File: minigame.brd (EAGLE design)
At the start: 98.7 x 80 mm, 37 parts, among them J1 AVR_SPI_PRG_6PTH, U1 MCP73831, U2 MIC5219 3.3V, Y1 8MHz

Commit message: Vista preliminar de la placa (BRD)
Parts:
- moved C6 105.0 mm to (35.6, 26.7)
- moved C7 100.4 mm to (30.5, 19.1)
- moved C8 99.8 mm to (30.5, 14.0)
- moved C9 99.8 mm to (30.5, 10.2)
- moved R11 92.6 mm to (26.7, 27.9)
- moved Y1 87.0 mm to (48.3, 33.0)
- moved U2 86.1 mm to (12.7, 29.2)
- moved R3 73.8 mm to (25.4, 58.4)
- moved R2 69.2 mm to (25.4, 62.2)
- moved C4 69.1 mm to (5.08, 30.5)
- moved C5 64.9 mm to (6.35, 16.5)
- moved R1 64.8 mm to (25.4, 66.0)
- moved U1 62.7 mm to (6.35, 24.1)
- moved J1 60.8 mm to (22.9, 72.4)
- moved R10 57.6 mm to (5.08, 8.89)
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
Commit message: ERC
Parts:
- LED1: value (none) -> RED
- OLED128X64: value (none) -> ADAFRUIT-938
- POWER: value (none) -> ON/OFF
- renumbered OLED128X64-938 to OLED128X64
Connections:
- removed net N$3: R1.1, S1.3, U$1.13
- net GND: now also BAT1.2; no longer BAT1.3
- net RST: now also R1.1, S1.3, U$1.13
- net VBAT: now also BAT1.3; no longer BAT1.2
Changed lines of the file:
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@@
 <element name="J1" library="SparkFun-Connectors" package="2X3" value="AVR_SPI_PRG_6PTH" x="22.86" y="72.39"/>
 <element name="JP1" library="SparkFun-Connectors" package="USB-MINIB-NOSTOP" value="USB-SMD-NS" x="49.53" y="5.08" rot="R90"/>
-<element name="LED1" library="SparkFun-LED" package="LED-0603" value="" x="6.35" y="60.96"/>
-<element name="OLED128X64-938" library="SparkFun-Connectors" package="1X08_LONGPADS" value="" x="38.1" y="68.58"/>
+<element name="LED1" library="SparkFun-LED" package="LED-0603" value="RED" x="6.35" y="60.96"/>
+<element name="OLED128X64" library="SparkFun-Connectors" package="1X08_LONGPADS" value="ADAFRUIT-938" x="38.1" y="68.58"/>
 <element name="R1" library="rcl" package="M0805" value="10k" x="25.4" y="66.04"/>
 <element name="R2" library="rcl" package="M0805" value="22" x="25.4" y="62.23"/>
@@
 <element name="R8" library="rcl" package="M0805" value="10k" x="20.32" y="7.62"/>
 <element name="R9" library="rcl" package="M0805" value="10k" x="20.32" y="3.81"/>
-<element name="POWER" library="SparkFun-Electromechanical" package="AYZ0202" value="" x="90.17" y="7.62">
+<element name="POWER" library="SparkFun-Electromechanical" package="AYZ0202" value="ON/OFF" x="90.17" y="7.62">
 <attribute name="PROD_ID" value="SWCH-08179" x="90.17" y="7.62" size="1.778" layer="27" display="off"/>
 </element>
@@
 <contactref element="R6" pad="1"/>
 <contactref element="R5" pad="1"/>
-<contactref element="BAT1" pad="3"/>
 <contactref element="U1" pad="2"/>
 <contactref element="R10" pad="2"/>
@@
 <contactref element="C9" pad="1"/>
 <contactref element="C8" pad="1"/>
-<wire x1="52.79" y1="49.72" x2="69.85" y2="66.04" width="0" layer="19" extent="1-1"/>
+<contactref element="BAT1" pad="2"/>
+<wire x1="52.79" y1="49.72" x2="82.55" y2="66.04" width="0" layer="19" extent="1-16"/>
 <wire x1="50.19" y1="51.52" x2="52.79" y2="49.72" width="0" layer="19" extent="1-1"/>
 <wire x1="43.79" y1="51.52" x2="50.19" y2="51.52" width="0" layer="19" extent="1-1"/>
@@
 <wire x1="45.39" y1="39.92" x2="41.19" y2="46.52" width="0" layer="19" extent="1-1"/>
 <wire x1="52.79" y1="41.72" x2="45.39" y2="39.92" width="0" layer="19" extent="1-1"/>
-<wire x1="19.37" y1="22.86" x2="45.39" y2="39.92" width="0" layer="19" extent="1-1"/>
-<wire x1="19.37" y1="19.05" x2="19.37" y2="22.86" width="0" layer="19" extent="1-1"/>
+<wire x1="33.16" y1="26.67" x2="45.39" y2="39.92" width="0" layer="19" extent="1-1"/>
+<wire x1="29.08" y1="19.05" x2="33.16" y2="26.67" width="0" layer="19" extent="1-1"/>
+<wire x1="29.08" y1="13.97" x2="29.08" y2="19.05" width="0" layer="19" extent="1-1"/>
+<wire x1="29.08" y1="10.16" x2="29.08" y2="13.97" width="0" layer="19" extent="1-1"/>
+<wire x1="19.37" y1="19.05" x2="29.08" y2="19.05" width="0" layer="19" extent="1-1"/>
+<wire x1="19.37" y1="22.86" x2="19.37" y2="19.05" width="0" layer="19" extent="1-1"/>
 <wire x1="19.37" y1="15.24" x2="19.37" y2="19.05" width="0" layer="19" extent="1-1"/>
 <wire x1="19.37" y1="11.43" x2="19.37" y2="15.24" width="0" layer="19" extent="1-1"/>
 <wire x1="19.37" y1="7.62" x2="19.37" y2="11.43" width="0" layer="19" extent="1-1"/>
 <wire x1="19.37" y1="3.81" x2="19.37" y2="7.62" width="0" layer="19" extent="1-1"/>
-<wire x1="51.13" y1="7.58" x2="19.37" y2="7.62" width="0" layer="19" extent="1-1"/>
-<wire x1="6.096" y1="76.835" x2="43.79" y2="51.52" width="0" layer="19" extent="1-1"/>
-<wire x1="15.11" y1="58.42" x2="6.096" y2="76.835" width="0" layer="19" extent="1-1"/>
-<wire x1="15.11" y1="62.23" x2="15.11" y2="58.42" width="0" layer="19" extent="1-1"/>
-<wire x1="15.11" y1="66.04" x2="15.11" y2="62.23" width="0" layer="19" extent="1-1"/>
-<wire x1="27.94" y1="74.93" x2="15.11" y2="58.42" width="0" layer="19" extent="1-1"/>
-<wire x1="6.35" y1="22.8299" x2="27.94" y2="74.93" width="0" layer="19" extent="1-1"/>
-<wire x1="6.03" y1="8.89" x2="6.35" y2="22.8299" width="0" layer="19" extent="1-1"/>
-<wire x1="3.68" y1="30.48" x2="6.03" y2="8.89" width="0" layer="19" extent="1-1"/>
-<wire x1="3.95" y1="16.51" x2="3.68" y2="30.48" width="0" layer="19" extent="1-1"/>
-<wire x1="12.7" y1="27.9099" x2="3.95" y2="16.51" width="0" layer="19" extent="1-1"/>
-<wire x1="33.16" y1="26.67" x2="12.7" y2="27.9099" width="0" layer="19" extent="1-1"/>
-<wire x1="29.08" y1="19.05" x2="33.16" y2="26.67" width="0" layer="19" extent="1-1"/>
-<wire x1="29.08" y1="13.97" x2="29.08" y2="19.05" width="0" layer="19" extent="1-1"/>
-<wire x1="29.08" y1="10.16" x2="29.08" y2="13.97" width="0" layer="19" extent="1-1"/>
+<wire x1="12.7" y1="27.9099" x2="19.37" y2="22.86" width="0" layer="19" extent="1-1"/>
+<wire x1="6.35" y1="22.8299" x2="12.7" y2="27.9099" width="0" layer="19" extent="1-1"/>
+<wire x1="3.95" y1="16.51" x2="6.35" y2="22.8299" width="0" layer="19" extent="1-1"/>
+<wire x1="6.03" y1="8.89" x2="3.95" y2="16.51" width="0" layer="19" extent="1-1"/>
+<wire x1="3.68" y1="30.48" x2="6.35" y2="22.8299" width="0" layer="19" extent="1-1"/>
+<wire x1="51.13" y1="7.58" x2="29.08" y2="10.16" width="0" layer="19" extent="1-1"/>
+<wire x1="27.94" y1="74.93" x2="43.79" y2="51.52" width="0" layer="19" extent="1-1"/>
+<wire x1="15.11" y1="66.04" x2="27.94" y2="74.93" width="0" layer="19" extent="1-1"/>
+<wire x1="15.11" y1="62.23" x2="15.11" y2="66.04" width="0" layer="19" extent="1-1"/>
+<wire x1="15.11" y1="58.42" x2="15.11" y2="62.23" width="0" layer="19" extent="1-1"/>
+<wire x1="6.096" y1="76.835" x2="15.11" y2="66.04" width="0" layer="19" extent="1-1"/>
 </signal>
 <signal name="3.3V">
@@
 <wire x1="6.48" y1="30.48" x2="7.3" y2="25.4301" width="0" layer="19" extent="1-1"/>
 </signal>
-<signal name="N$3">
-<contactref element="R1" pad="1"/>
-<contactref element="S1" pad="3"/>
-<contactref element="U$1" pad="13"/>
-<wire x1="24.45" y1="66.04" x2="6.096" y2="73.025" width="0" layer="19" extent="1-1"/>
-<wire x1="43.79" y1="39.92" x2="24.45" y2="66.04" width="0" layer="19" extent="1-1"/>
-</signal>
 <signal name="D-">
 <contactref element="R2" pad="1"/>
@@
 <signal name="RST">
 <contactref element="J1" pad="5"/>
+<contactref element="R1" pad="1"/>
+<contactref element="S1" pad="3"/>
+<contactref element="U$1" pad="13"/>
+<wire x1="24.45" y1="66.04" x2="27.94" y2="72.39" width="0" layer="19" extent="1-1"/>
+<wire x1="6.096" y1="73.025" x2="24.45" y2="66.04" width="0" layer="19" extent="1-1"/>
+<wire x1="43.79" y1="39.92" x2="24.45" y2="66.04" width="0" layer="19" extent="1-1"/>
 </signal>
 <signal name="MOSI">
@@
 </signal>
 <signal name="OLED_DATA">
-<contactref element="OLED128X64-938" pad="1"/>
+<contactref element="OLED128X64" pad="1"/>
 </signal>
 <signal name="OLED_CLK">
-<contactref element="OLED128X64-938" pad="2"/>
+<contactref element="OLED128X64" pad="2"/>
 </signal>
 <signal name="OLED_DC">
-<contactref element="OLED128X64-938" pad="3"/>
+<contactref element="OLED128X64" pad="3"/>
 </signal>
 <signal name="OLED_RST">
-<contactref element="OLED128X64-938" pad="4"/>
+<contactref element="OLED128X64" pad="4"/>
 </signal>
 <signal name="OLED_CS">
-<contactref element="OLED128X64-938" pad="5"/>
+<contactref element="OLED128X64" pad="5"/>
 </signal>
 <signal name="OLED_3V3">
-<contactref element="OLED128X64-938" pad="6"/>
+<contactref element="OLED128X64" pad="6"/>
 </signal>
 <signal name="OLED_VIN">
-<contactref element="OLED128X64-938" pad="7"/>
+<contactref element="OLED128X64" pad="7"/>
 </signal>
 <signal name="OLED_GND">
-<contactref element="OLED128X64-938" pad="8"/>
+<contactref element="OLED128X64" pad="8"/>
 </signal>
 <signal name="UP">
@@
 <wire x1="5.4" y1="25.4301" x2="4.13" y2="8.89" width="0" layer="19" extent="1-1"/>
 </signal>
-<signal name="VBAT">
-<contactref element="U1" pad="3"/>
-<contactref element="BAT1" pad="2"/>
-<contactref element="C5" pad="+"/>
-<contactref element="POWER" pad="2"/>
-<wire x1="90.17" y1="10.445" x2="82.55" y2="66.04" width="0" layer="19" extent="1-16"/>
-<wire x1="8.75" y1="16.51" x2="90.17" y2="10.445" width="0" layer="19" extent="1-1"/>
-<wire x1="7.3" y1="22.8299" x2="8.75" y2="16.51" width="0" layer="19" extent="1-1"/>
-</signal>
 <signal name="CHARGE">
 <contactref element="U$1" pad="32"/>
@@
 <wire x1="13.65" y1="30.5101" x2="31.88" y2="19.05" width="0" layer="19" extent="1-1"/>
 </signal>
+<signal name="VBAT">
+<contactref element="U1" pad="3"/>
+<contactref element="C5" pad="+"/>
+<contactref element="POWER" pad="2"/>
+<contactref element="BAT1" pad="3"/>
+<wire x1="90.17" y1="10.445" x2="69.85" y2="66.04" width="0" layer="19" extent="1-1"/>
+<wire x1="7.3" y1="22.8299" x2="69.85" y2="66.04" width="0" layer="19" extent="1-1"/>
+<wire x1="8.75" y1="16.51" x2="7.3" y2="22.8299" width="0" layer="19" extent="1-1"/>
+</signal>
 </signals>

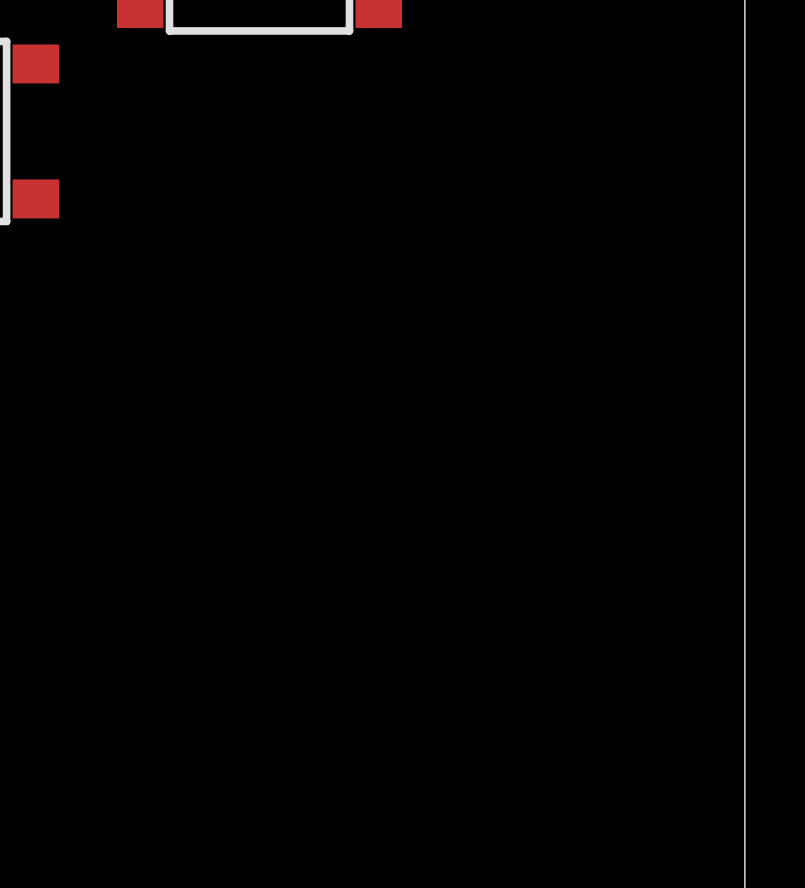
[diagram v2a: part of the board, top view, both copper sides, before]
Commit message: Added OLED wires Added buzzer circuit
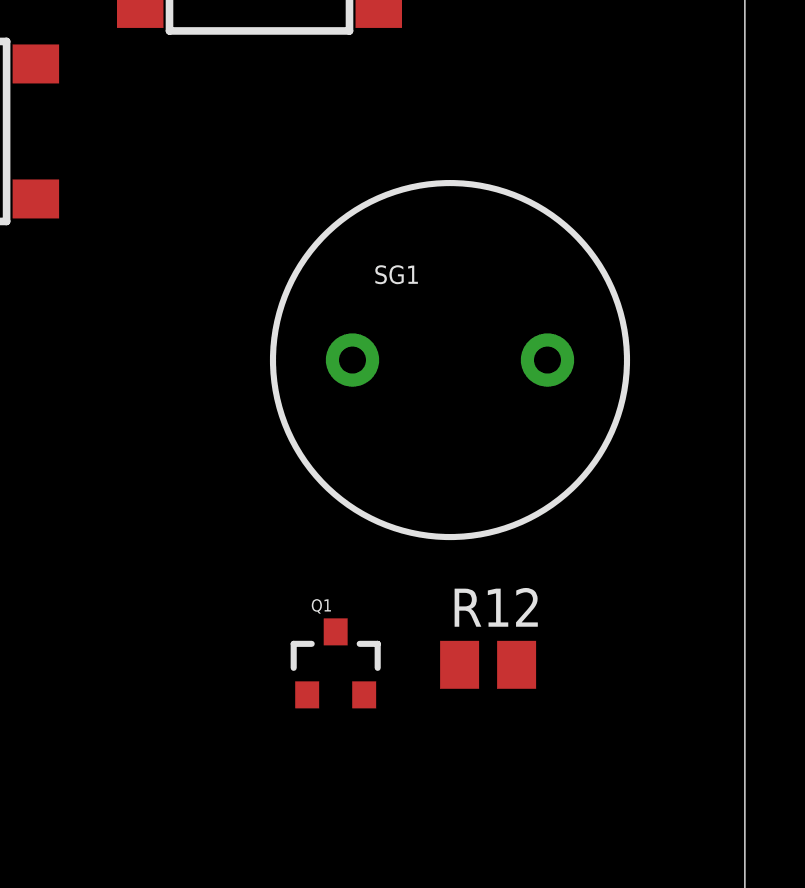
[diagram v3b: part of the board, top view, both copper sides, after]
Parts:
- added Q1: MMBT2222A, SparkFun-DiscreteSemi:SOT23-3
- added R12: 180, rcl:M0805
- added SG1: BUZZERPTH, SparkFun-Electromechanical:BUZZER-12MM
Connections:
- removed net OLED_GND: OLED128X64.8
- removed net OLED_VIN: OLED128X64.7
- new net BUZZER: R12.2, U$1.18
- new net N$11: Q1.1, R12.1
- new net N$3: Q1.3, SG1.-
- net 3.3V: now also OLED128X64.7, SG1.+
- net A: now also U$1.27; no longer U$1.28
- net B: now also U$1.1; no longer U$1.29
- net CHARGE: now also U$1.28; no longer U$1.32
- net DOWN: now also U$1.19; no longer U$1.31
- net GND: now also OLED128X64.8, Q1.2
- net LEFT: now also U$1.25; no longer U$1.27
- net OLED_CLK: now also U$1.30
- net OLED_CS: now also U$1.26
- net OLED_DATA: now also U$1.29
- net OLED_DC: now also U$1.12
- net OLED_RST: now also U$1.32
- net RIGHT: now also U$1.31; no longer U$1.1
- net UP: now also U$1.21; no longer U$1.25
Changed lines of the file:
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@@
 <element name="C8" library="SparkFun-Passives" package="1206" value="1uF" x="30.48" y="13.97"/>
 <element name="C9" library="SparkFun-Passives" package="1206" value="0.1uF" x="30.48" y="10.16"/>
+<element name="SG1" library="SparkFun-Electromechanical" package="BUZZER-12MM" value="BUZZERPTH" x="88.9" y="33.02"/>
+<element name="Q1" library="SparkFun-DiscreteSemi" package="SOT23-3" value="MMBT2222A" x="85.09" y="22.86">
+<attribute name="PROD_ID" value="TRANS-08049" x="85.09" y="22.86" size="1.778" layer="27" display="off"/>
+</element>
+<element name="R12" library="rcl" package="M0805" value="180" x="90.17" y="22.86"/>
 </elements>
 <signals>
@@
 <contactref element="C8" pad="1"/>
 <contactref element="BAT1" pad="2"/>
-<wire x1="52.79" y1="49.72" x2="82.55" y2="66.04" width="0" layer="19" extent="1-16"/>
-<wire x1="50.19" y1="51.52" x2="52.79" y2="49.72" width="0" layer="19" extent="1-1"/>
+<contactref element="OLED128X64" pad="8"/>
+<contactref element="Q1" pad="2"/>
+<wire x1="55.88" y1="68.58" x2="82.55" y2="66.04" width="0" layer="19" extent="16-16"/>
+<wire x1="50.19" y1="51.52" x2="55.88" y2="68.58" width="0" layer="19" extent="1-1"/>
+<wire x1="52.79" y1="49.72" x2="50.19" y2="51.52" width="0" layer="19" extent="1-1"/>
 <wire x1="43.79" y1="51.52" x2="50.19" y2="51.52" width="0" layer="19" extent="1-1"/>
 <wire x1="41.19" y1="46.52" x2="43.79" y2="51.52" width="0" layer="19" extent="1-1"/>
@@
 <wire x1="3.68" y1="30.48" x2="6.35" y2="22.8299" width="0" layer="19" extent="1-1"/>
 <wire x1="51.13" y1="7.58" x2="29.08" y2="10.16" width="0" layer="19" extent="1-1"/>
+<wire x1="86.04" y1="21.86" x2="6.03" y2="8.89" width="0" layer="19" extent="1-1"/>
 <wire x1="27.94" y1="74.93" x2="43.79" y2="51.52" width="0" layer="19" extent="1-1"/>
 <wire x1="15.11" y1="66.04" x2="27.94" y2="74.93" width="0" layer="19" extent="1-1"/>
@@
 <contactref element="U2" pad="5"/>
 <contactref element="C9" pad="2"/>
+<contactref element="OLED128X64" pad="7"/>
+<contactref element="SG1" pad="+"/>
 <wire x1="75.095" y1="38.39" x2="86.525" y2="44.74" width="0" layer="19" extent="1-1"/>
 <wire x1="52.79" y1="42.52" x2="75.095" y2="38.39" width="0" layer="19" extent="1-1"/>
@@
 <wire x1="50.99" y1="51.52" x2="52.79" y2="42.52" width="0" layer="19" extent="1-1"/>
 <wire x1="42.99" y1="51.52" x2="50.99" y2="51.52" width="0" layer="19" extent="1-1"/>
+<wire x1="37.96" y1="26.67" x2="44.59" y2="39.92" width="0" layer="19" extent="1-1"/>
+<wire x1="31.88" y1="13.97" x2="37.96" y2="26.67" width="0" layer="19" extent="1-1"/>
+<wire x1="31.88" y1="10.16" x2="31.88" y2="13.97" width="0" layer="19" extent="1-1"/>
+<wire x1="53.34" y1="68.58" x2="50.99" y2="51.52" width="0" layer="19" extent="1-1"/>
 <wire x1="25.565" y1="42.2" x2="44.59" y2="39.92" width="0" layer="19" extent="1-1"/>
 <wire x1="17.945" y1="49.82" x2="25.565" y2="42.2" width="0" layer="19" extent="1-1"/>
 <wire x1="17.945" y1="34.58" x2="25.565" y2="42.2" width="0" layer="19" extent="1-1"/>
+<wire x1="11.75" y1="30.5101" x2="17.945" y2="34.58" width="0" layer="19" extent="1-1"/>
 <wire x1="10.325" y1="42.2" x2="17.945" y2="49.82" width="0" layer="19" extent="1-1"/>
-<wire x1="22.86" y1="74.93" x2="10.325" y2="42.2" width="0" layer="19" extent="1-1"/>
-<wire x1="26.35" y1="66.04" x2="22.86" y2="74.93" width="0" layer="19" extent="1-1"/>
-<wire x1="11.75" y1="30.5101" x2="22.86" y2="74.93" width="0" layer="19" extent="1-1"/>
-<wire x1="37.96" y1="26.67" x2="11.75" y2="30.5101" width="0" layer="19" extent="1-1"/>
-<wire x1="31.88" y1="13.97" x2="37.96" y2="26.67" width="0" layer="19" extent="1-1"/>
-<wire x1="31.88" y1="10.16" x2="31.88" y2="13.97" width="0" layer="19" extent="1-1"/>
+<wire x1="26.35" y1="66.04" x2="17.945" y2="49.82" width="0" layer="19" extent="1-1"/>
+<wire x1="22.86" y1="74.93" x2="26.35" y2="66.04" width="0" layer="19" extent="1-1"/>
+<wire x1="92.15" y1="33.02" x2="31.88" y2="10.16" width="0" layer="19" extent="1-1"/>
 </signal>
 <signal name="N$4">
@@
 <signal name="OLED_DATA">
 <contactref element="OLED128X64" pad="1"/>
+<contactref element="U$1" pad="29"/>
+<wire x1="52.79" y1="46.52" x2="38.1" y2="68.58" width="0" layer="19" extent="1-1"/>
 </signal>
 <signal name="OLED_CLK">
 <contactref element="OLED128X64" pad="2"/>
+<contactref element="U$1" pad="30"/>
+<wire x1="52.79" y1="47.32" x2="40.64" y2="68.58" width="0" layer="19" extent="1-1"/>
 </signal>
 <signal name="OLED_DC">
 <contactref element="OLED128X64" pad="3"/>
+<contactref element="U$1" pad="12"/>
+<wire x1="42.99" y1="39.92" x2="43.18" y2="68.58" width="0" layer="19" extent="1-1"/>
 </signal>
 <signal name="OLED_RST">
 <contactref element="OLED128X64" pad="4"/>
+<contactref element="U$1" pad="32"/>
+<wire x1="52.79" y1="48.92" x2="45.72" y2="68.58" width="0" layer="19" extent="1-1"/>
 </signal>
 <signal name="OLED_CS">
 <contactref element="OLED128X64" pad="5"/>
+<contactref element="U$1" pad="26"/>
+<wire x1="52.79" y1="44.12" x2="48.26" y2="68.58" width="0" layer="19" extent="1-1"/>
 </signal>
 <signal name="OLED_3V3">
 <contactref element="OLED128X64" pad="6"/>
 </signal>
-<signal name="OLED_VIN">
-<contactref element="OLED128X64" pad="7"/>
-</signal>
-<signal name="OLED_GND">
-<contactref element="OLED128X64" pad="8"/>
-</signal>
 <signal name="UP">
 <contactref element="R4" pad="2"/>
-<contactref element="U$1" pad="25"/>
 <contactref element="S9" pad="B2"/>
-<wire x1="21.27" y1="22.86" x2="17.945" y2="54.32" width="0" layer="19" extent="1-1"/>
-<wire x1="52.79" y1="43.32" x2="21.27" y2="22.86" width="0" layer="19" extent="1-1"/>
+<contactref element="U$1" pad="21"/>
+<wire x1="21.27" y1="22.86" x2="50.19" y2="39.92" width="0" layer="19" extent="1-1"/>
+<wire x1="17.945" y1="54.32" x2="21.27" y2="22.86" width="0" layer="19" extent="1-1"/>
 </signal>
 <signal name="DOWN">
 <contactref element="R5" pad="2"/>
-<contactref element="U$1" pad="31"/>
 <contactref element="S2" pad="B2"/>
+<contactref element="U$1" pad="19"/>
+<wire x1="17.945" y1="39.08" x2="48.59" y2="39.92" width="0" layer="19" extent="1-1"/>
 <wire x1="21.27" y1="19.05" x2="17.945" y2="39.08" width="0" layer="19" extent="1-1"/>
-<wire x1="52.79" y1="48.12" x2="21.27" y2="19.05" width="0" layer="19" extent="1-1"/>
 </signal>
 <signal name="LEFT">
 <contactref element="R6" pad="2"/>
-<contactref element="U$1" pad="27"/>
 <contactref element="S3" pad="B2"/>
-<wire x1="21.27" y1="15.24" x2="10.325" y2="46.7" width="0" layer="19" extent="1-1"/>
-<wire x1="52.79" y1="44.92" x2="21.27" y2="15.24" width="0" layer="19" extent="1-1"/>
+<contactref element="U$1" pad="25"/>
+<wire x1="21.27" y1="15.24" x2="52.79" y2="43.32" width="0" layer="19" extent="1-1"/>
+<wire x1="10.325" y1="46.7" x2="21.27" y2="15.24" width="0" layer="19" extent="1-1"/>
 </signal>
 <signal name="RIGHT">
 <contactref element="R7" pad="2"/>
-<contactref element="U$1" pad="1"/>
 <contactref element="S4" pad="B2"/>
+<contactref element="U$1" pad="31"/>
+<wire x1="25.565" y1="46.7" x2="52.79" y2="48.12" width="0" layer="19" extent="1-1"/>
 <wire x1="21.27" y1="11.43" x2="25.565" y2="46.7" width="0" layer="19" extent="1-1"/>
-<wire x1="41.19" y1="49.72" x2="21.27" y2="11.43" width="0" layer="19" extent="1-1"/>
 </signal>
 <signal name="A">
 <contactref element="R8" pad="2"/>
-<contactref element="U$1" pad="28"/>
 <contactref element="S5" pad="B2"/>
-<wire x1="21.27" y1="7.62" x2="75.095" y2="42.89" width="0" layer="19" extent="1-1"/>
-<wire x1="52.79" y1="45.72" x2="21.27" y2="7.62" width="0" layer="19" extent="1-1"/>
+<contactref element="U$1" pad="27"/>
+<wire x1="52.79" y1="44.92" x2="75.095" y2="42.89" width="0" layer="19" extent="1-1"/>
+<wire x1="21.27" y1="7.62" x2="52.79" y2="44.92" width="0" layer="19" extent="1-1"/>
 </signal>
 <signal name="B">
 <contactref element="R9" pad="2"/>
-<contactref element="U$1" pad="29"/>
 <contactref element="S6" pad="B2"/>
-<wire x1="21.27" y1="3.81" x2="86.525" y2="49.24" width="0" layer="19" extent="1-1"/>
-<wire x1="52.79" y1="46.52" x2="21.27" y2="3.81" width="0" layer="19" extent="1-1"/>
+<contactref element="U$1" pad="1"/>
+<wire x1="41.19" y1="49.72" x2="86.525" y2="49.24" width="0" layer="19" extent="1-1"/>
+<wire x1="21.27" y1="3.81" x2="41.19" y2="49.72" width="0" layer="19" extent="1-1"/>
 </signal>
 <signal name="N$7">
@@
 </signal>
 <signal name="CHARGE">
-<contactref element="U$1" pad="32"/>
 <contactref element="U1" pad="1"/>
 <contactref element="R11" pad="1"/>
-<wire x1="5.4" y1="22.8299" x2="52.79" y2="48.92" width="0" layer="19" extent="1-1"/>
-<wire x1="25.72" y1="27.94" x2="5.4" y2="22.8299" width="0" layer="19" extent="1-1"/>
+<contactref element="U$1" pad="28"/>
+<wire x1="25.72" y1="27.94" x2="52.79" y2="45.72" width="0" layer="19" extent="1-1"/>
+<wire x1="5.4" y1="22.8299" x2="25.72" y2="27.94" width="0" layer="19" extent="1-1"/>
 </signal>
 <signal name="N$9">
@@
 <wire x1="8.75" y1="16.51" x2="7.3" y2="22.8299" width="0" layer="19" extent="1-1"/>
 </signal>
+<signal name="N$3">
+<contactref element="SG1" pad="-"/>
+<contactref element="Q1" pad="3"/>
+<wire x1="85.65" y1="33.02" x2="85.09" y2="23.96" width="0" layer="19" extent="1-1"/>
+</signal>
+<signal name="N$11">
+<contactref element="R12" pad="1"/>
+<contactref element="Q1" pad="1"/>
+<wire x1="84.14" y1="21.86" x2="89.22" y2="22.86" width="0" layer="19" extent="1-1"/>
+</signal>
+<signal name="BUZZER">
+<contactref element="U$1" pad="18"/>
+<contactref element="R12" pad="2"/>
+<wire x1="91.12" y1="22.86" x2="47.79" y2="39.92" width="0" layer="19" extent="1-1"/>
+</signal>
 </signals>
